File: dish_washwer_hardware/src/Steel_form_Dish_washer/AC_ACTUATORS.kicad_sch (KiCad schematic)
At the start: 61 parts, among them J10 DRAIN PUMP CONNECTOR, J11 WASH PUMP CONNECTOR, J12 BOILER HEATER CONNECTOR, J13 TANK HEATER, J14 peristaltic_pump_2, J15 peristaltic_pump_1, J7 Water sensor connector, J9 SOLENOID CONNECTOR, K1 9-1440003-0, K2 9-1440003-0, K3 9-1440003-0, K4 9-1440003-0, Q3 WST2N7002K, Q4 WST2N7002K, Q5 WST2N7002K, U10 MOC3021, U11 MOC3021, U12 MOC3021, U14 9-1393243-3, U5 9-1393243-3, U6 HCPL3700M, U7 MOC3021, U8 MOC3021, U9 MOC3021

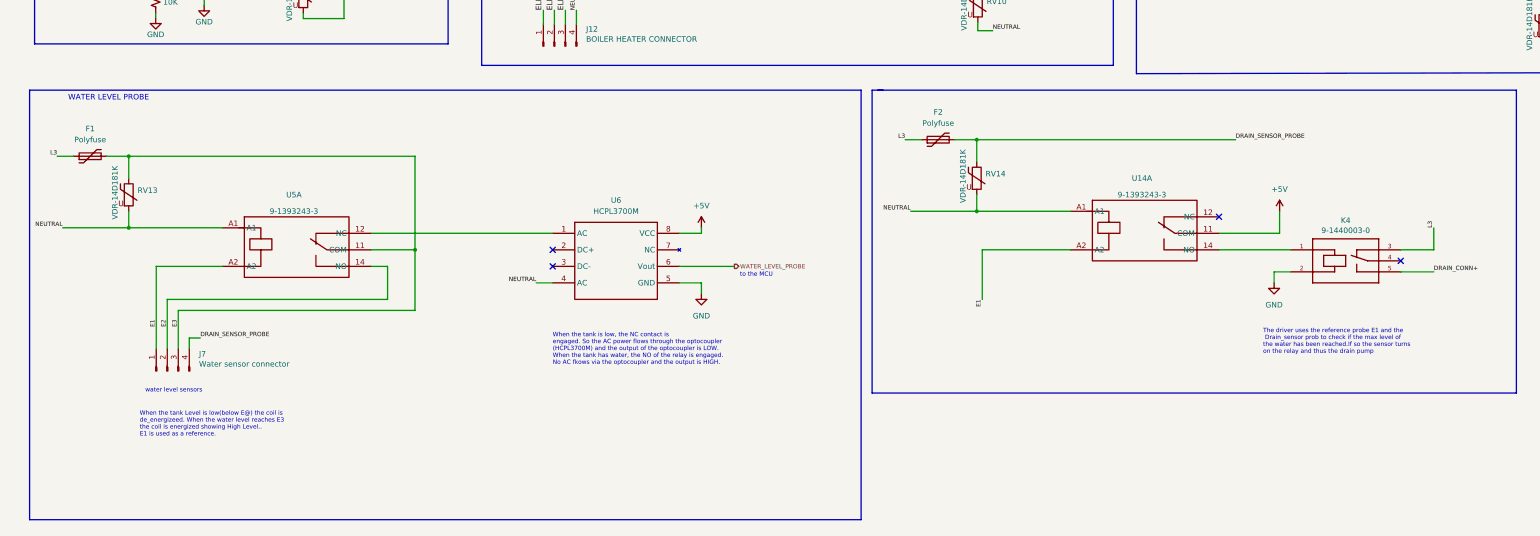
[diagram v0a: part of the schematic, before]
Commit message: updated water level sensor
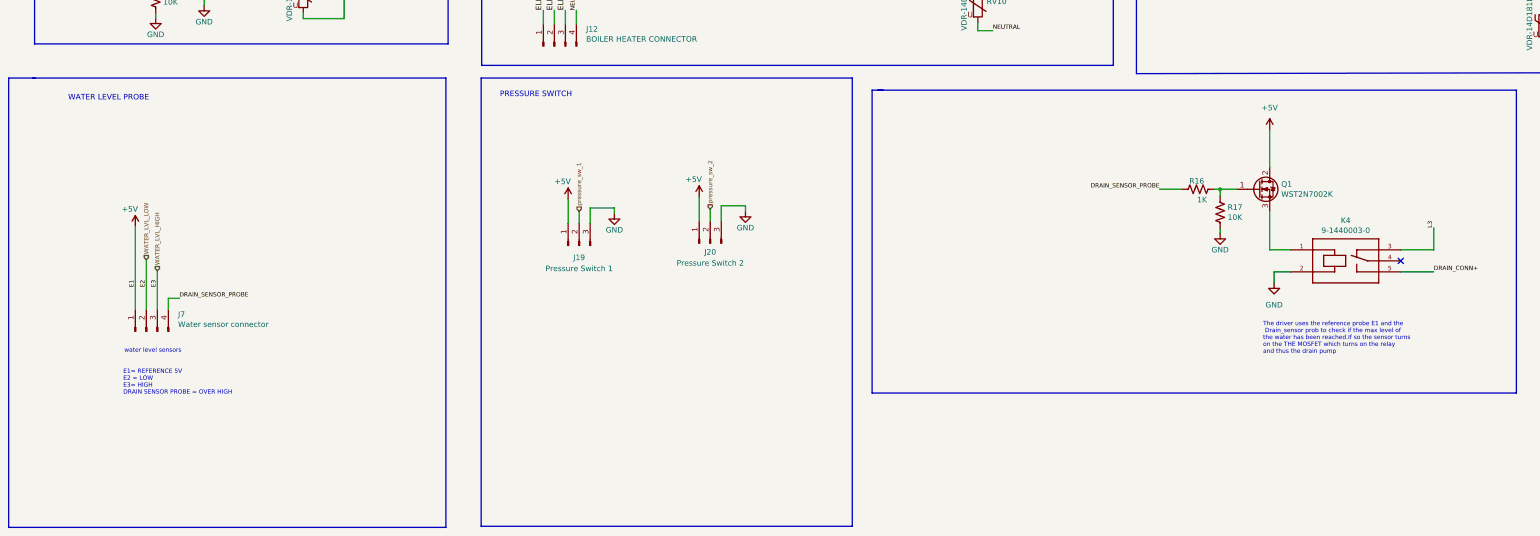
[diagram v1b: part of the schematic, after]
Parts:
- removed F1, F2: Polyfuse, greencharge-footprints:BK250-600, symbol Device:Polyfuse
- removed RV13, RV14: VDR-14D181K, Varistor:RV_Disc_D16.5mm_W6.7mm_P7.5mm, symbol Device:Varistor
- removed U14, U5: 9-1393243-3, greencharge-footprints:9-1393243-3, symbol GCL_Relays_Coils:9-1393243-3
- removed U6: HCPL3700M, Package_DIP:DIP-8_W7.62mm, symbol GCL_Integrated-Circuits:HCPL3700M
- added J19: Pressure Switch 1, Connector_JST:JST_EH_S3B-EH_1x03_P2.50mm_Horizontal, symbol Connector:Conn_01x03_Male
- added J20: Pressure Switch 2, Connector_JST:JST_EH_S3B-EH_1x03_P2.50mm_Horizontal, symbol Connector:Conn_01x03_Male
- added Q1: WST2N7002K, Package_TO_SOT_SMD:SOT-23, symbol Device:Q_NMOS_GDS
- added R16: 1K, Resistor_SMD:R_0402_1005Metric, symbol Device:R_US
- added R17: 10K, Resistor_SMD:R_0402_1005Metric, symbol Device:R_US
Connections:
- net E1 is gone; now on net +5V: J7.1 (Pin_1)
- net +5V: now also J19.1 (Pin_1), J20.1 (Pin_1), Q1.2 (D)
- net DRAIN_SENSOR_PROBE: now also R16.1
- net GND: now also J19.3 (Pin_3), J20.3 (Pin_3), R17.2
- net at K4.1: now also Q1.3 (S)
- net E2 renamed WATER_LVL_LOW
- net E3 renamed WATER_LVL_HIGH
- new net: Q1.1 (G), R16.2, R17.1
- new net pressure_sw_1: J19.2 (Pin_2)
- new net pressure_sw_2: J20.2 (Pin_2)
- no-connect marks 13 -> 10
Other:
- note added: "E1= REFERENCE 5V E2 = LOW E3= HIGH DRAIN SENSOR PROBE = OVER HIGH"
- note added: "PRESSURE SWITCH"
- note added: "The driver uses the reference probe E1 and the Drain_sensor prob to check if the max level of the water has been reached.If so the sensor turns on the THE MOSFET which turns on the relay and thus the drain pump"
- note removed: "The driver uses the reference probe E1 and the Drain_sensor prob to check if the max level of the water has been reached.If so the sensor turns on the relay and thus the drain pump"
- note removed: "When the tank Level is low(below E@) the coil is de_energizeed. When the water level reaches E3 the coil is energized showing High Level.. E1 is used as a reference."
- note removed: "When the tank is low, the NC contact is engaged. So the AC power flows through the optocoupler (HCPL3700M) and the output of the optocoupler is LOW. When the tank has water, the NO of the relay is engaged. No AC fkows via the optocoupler and the output is HIGH."
- note removed: "to the MCU"
- moved on the sheet: J7
